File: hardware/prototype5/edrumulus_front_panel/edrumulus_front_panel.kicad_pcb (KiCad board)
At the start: 2 copper layers, 65 x 56.5 mm, 2 parts, among them J2 Raspberry Pi GPIO pins

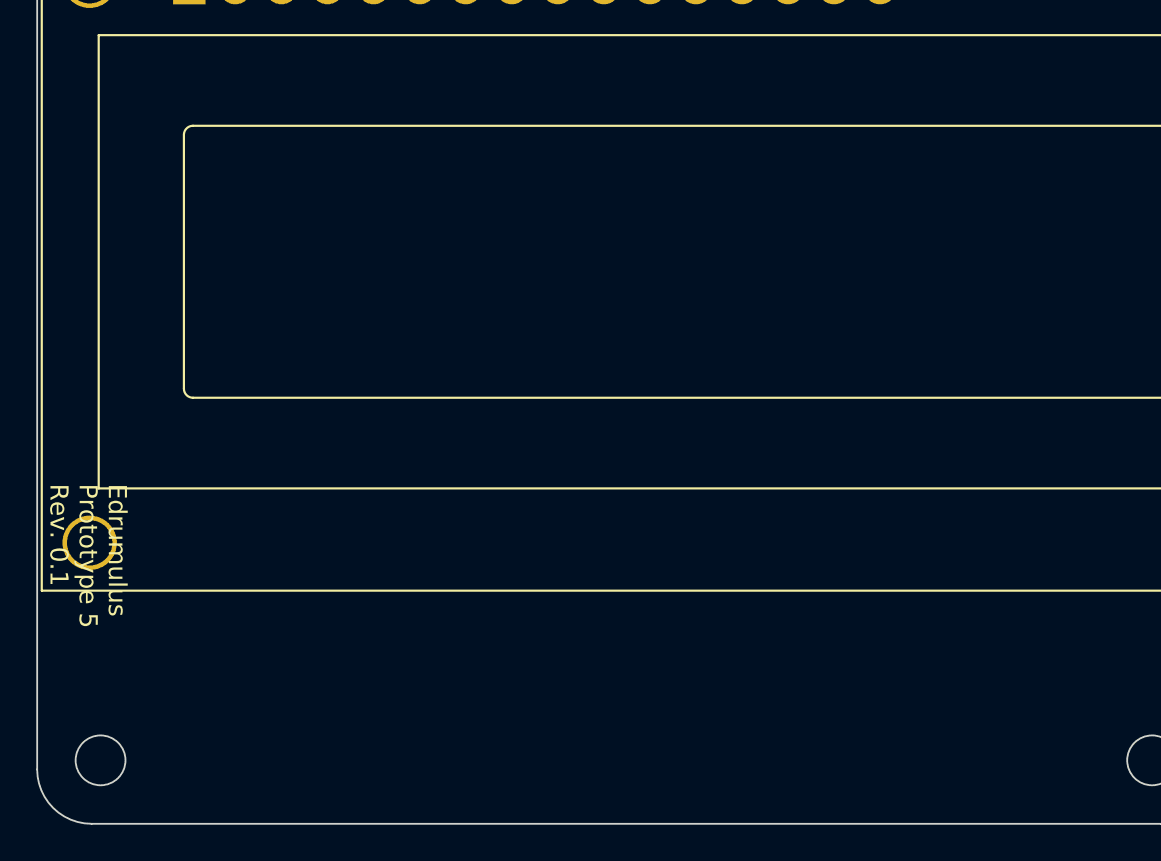
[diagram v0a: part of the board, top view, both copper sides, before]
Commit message: adding buttons to the front panel for prototype 5
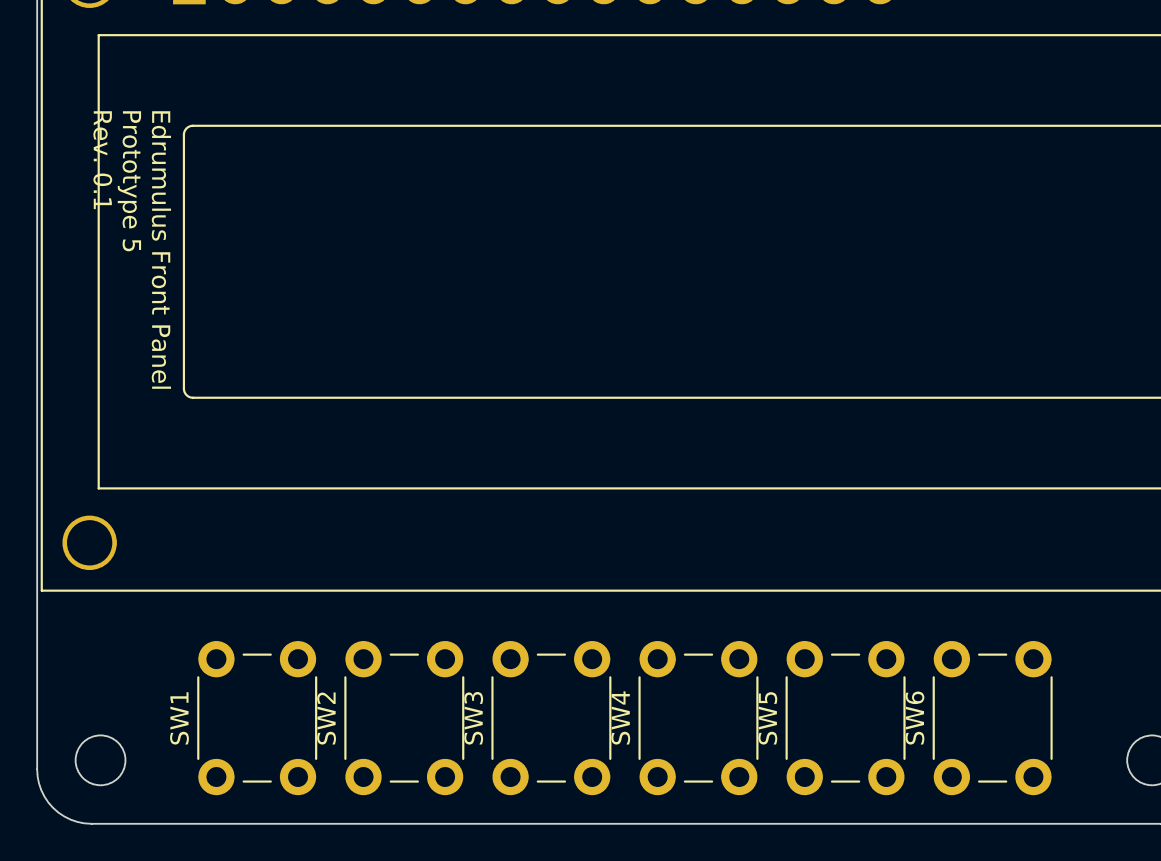
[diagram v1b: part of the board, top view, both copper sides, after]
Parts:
- added SW1: SW_Push, Button_Switch_THT:SW_PUSH_6mm_H7.3mm, F.Cu at (116.5, 127.0)
- added SW2: SW_Push, Button_Switch_THT:SW_PUSH_6mm_H7.3mm, F.Cu at (124.6, 127.0)
- added SW3: SW_Push, Button_Switch_THT:SW_PUSH_6mm_H7.3mm, F.Cu at (132.7, 127.0)
- added SW4: SW_Push, Button_Switch_THT:SW_PUSH_6mm_H7.3mm, F.Cu at (140.8, 127.0)
- added SW5: SW_Push, Button_Switch_THT:SW_PUSH_6mm_H7.3mm, F.Cu at (148.9, 127.0)
- added SW6: SW_Push, Button_Switch_THT:SW_PUSH_6mm_H7.3mm, F.Cu at (157.0, 127.0)
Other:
- board text added: "Edrumulus Front Panel Prototype 5 Rev. 0.1"
- board text removed: "Edrumulus Prototype 5 Rev. 0.1"

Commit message: work on display for prototype 5
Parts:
- added R1: 10k, Resistor_SMD:R_1206_3216Metric_Pad1.30x1.75mm_HandSolder, F.Cu at (111.8, 135.9)
- added R10: 1k, Resistor_SMD:R_1206_3216Metric_Pad1.30x1.75mm_HandSolder, F.Cu at (149.9, 113.0)
- added R11: 10k, Resistor_SMD:R_1206_3216Metric_Pad1.30x1.75mm_HandSolder, F.Cu at (150.8, 149.9)
- added R12: 1k, Resistor_SMD:R_1206_3216Metric_Pad1.30x1.75mm_HandSolder, F.Cu at (157.5, 113.0)
- added R13: 470, Resistor_SMD:R_1206_3216Metric_Pad1.30x1.75mm_HandSolder, F.Cu at (135.9, 88.9)
- added R2: 1k, Resistor_SMD:R_1206_3216Metric_Pad1.30x1.75mm_HandSolder, F.Cu at (116.8, 113.0)
- added R3: 10k, Resistor_SMD:R_1206_3216Metric_Pad1.30x1.75mm_HandSolder, F.Cu at (126.8, 137.2)
- added R4: 1k, Resistor_SMD:R_1206_3216Metric_Pad1.30x1.75mm_HandSolder, F.Cu at (124.5, 113.0)
- added R5: 10k, Resistor_SMD:R_1206_3216Metric_Pad1.30x1.75mm_HandSolder, F.Cu at (175.3, 141.0)
- added R6: 1k, Resistor_SMD:R_1206_3216Metric_Pad1.30x1.75mm_HandSolder, F.Cu at (133.3, 113.0)
- added R7: 10k, Resistor_SMD:R_1206_3216Metric_Pad1.30x1.75mm_HandSolder, F.Cu at (158.8, 144.8)
- added R8: 1k, Resistor_SMD:R_1206_3216Metric_Pad1.30x1.75mm_HandSolder, F.Cu at (141.0, 113.3)
- added R9: 10k, Resistor_SMD:R_1206_3216Metric_Pad1.30x1.75mm_HandSolder, F.Cu at (162.6, 135.9)
- added RV1: 10k, Potentiometer_THT:Potentiometer_ACP_CA9-H2,5_Horizontal, F.Cu at (184.2, 121.9)
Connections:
- DS1 pad 1: unconnected-(DS1-Pad1) -> GND
- DS1 pad 11: unconnected-(DS1-Pad11) -> PI-GPIO22
- DS1 pad 12: unconnected-(DS1-Pad12) -> PI-GPIO23
- DS1 pad 13: unconnected-(DS1-Pad13) -> PI-GPIO24
- DS1 pad 14: unconnected-(DS1-Pad14) -> PI-GPIO10
- DS1 pad 15: unconnected-(DS1-Pad15) -> Net-(DS1-Pad15)
- DS1 pad 16: unconnected-(DS1-Pad16) -> GND
- DS1 pad 2: unconnected-(DS1-Pad2) -> 5V
- DS1 pad 3: unconnected-(DS1-Pad3) -> Net-(RV1-Pad2)
- DS1 pad 4: unconnected-(DS1-Pad4) -> PI-GPIO27
- DS1 pad 5: unconnected-(DS1-Pad5) -> GND
- DS1 pad 6: unconnected-(DS1-Pad6) -> PI-GPIO17
- J2 pad 1: unconnected-(J2-Pad1) -> 3V3
- J2 pad 10: ESP-UART0-TX -> unconnected-(J2-Pad10)
- J2 pad 11: unconnected-(J2-Pad11) -> PI-GPIO17
- J2 pad 13: unconnected-(J2-Pad13) -> PI-GPIO27
- J2 pad 15: unconnected-(J2-Pad15) -> PI-GPIO22
- J2 pad 16: unconnected-(J2-Pad16) -> PI-GPIO23
- J2 pad 18: unconnected-(J2-Pad18) -> PI-GPIO24
- J2 pad 19: unconnected-(J2-Pad19) -> PI-GPIO10
- J2 pad 2: RASPI-VIN -> 5V
- J2 pad 21: PI-GPIO9 -> unconnected-(J2-Pad21)
- J2 pad 22: unconnected-(J2-Pad22) -> PI-GPIO25
- J2 pad 23: unconnected-(J2-Pad23) -> PI-GPIO11
- J2 pad 24: unconnected-(J2-Pad24) -> PI-GPIO8
- J2 pad 26: unconnected-(J2-Pad26) -> PI-GPIO7
- J2 pad 32: unconnected-(J2-Pad32) -> PI-GPIO12
- J2 pad 33: unconnected-(J2-Pad33) -> PI-GPIO13
- J2 pad 4: RASPI-VIN -> 5V
- J2 pad 7: PI-GPIO4 -> unconnected-(J2-Pad7)
- J2 pad 8: ESP-UART0-RX -> unconnected-(J2-Pad8)
- SW1 pad 1: unconnected-(SW1-Pad1) -> Net-(R1-Pad2)
- SW1 pad 2: unconnected-(SW1-Pad2) -> GND
- SW2 pad 1: unconnected-(SW2-Pad1) -> Net-(R3-Pad2)
- SW2 pad 2: unconnected-(SW2-Pad2) -> GND
- SW3 pad 1: unconnected-(SW3-Pad1) -> Net-(R5-Pad2)
- SW3 pad 2: unconnected-(SW3-Pad2) -> GND
- SW4 pad 1: unconnected-(SW4-Pad1) -> Net-(R7-Pad2)
- SW4 pad 2: unconnected-(SW4-Pad2) -> GND
- SW5 pad 1: unconnected-(SW5-Pad1) -> Net-(R10-Pad1)
- SW5 pad 2: unconnected-(SW5-Pad2) -> GND
- SW6 pad 1: unconnected-(SW6-Pad1) -> Net-(R11-Pad2)
- SW6 pad 2: unconnected-(SW6-Pad2) -> GND

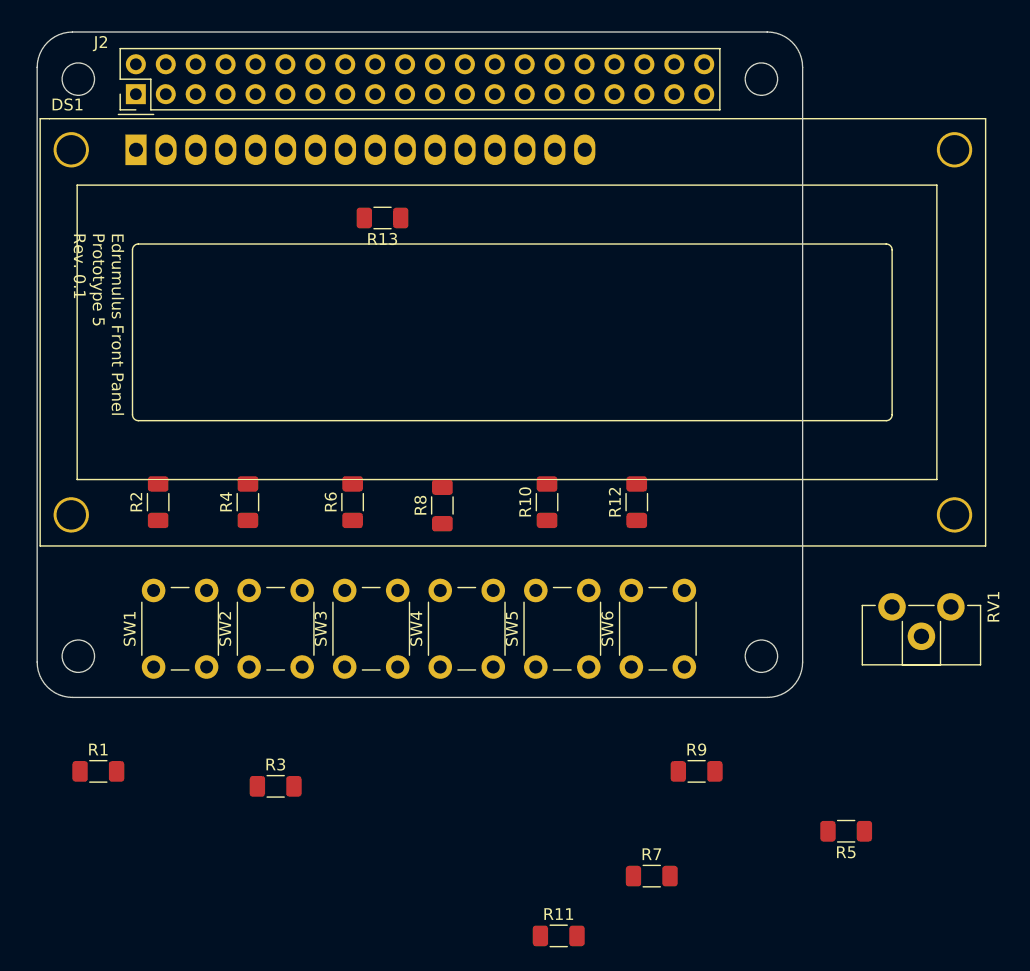
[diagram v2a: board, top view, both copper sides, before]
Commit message: finished display front panel for prototype 5
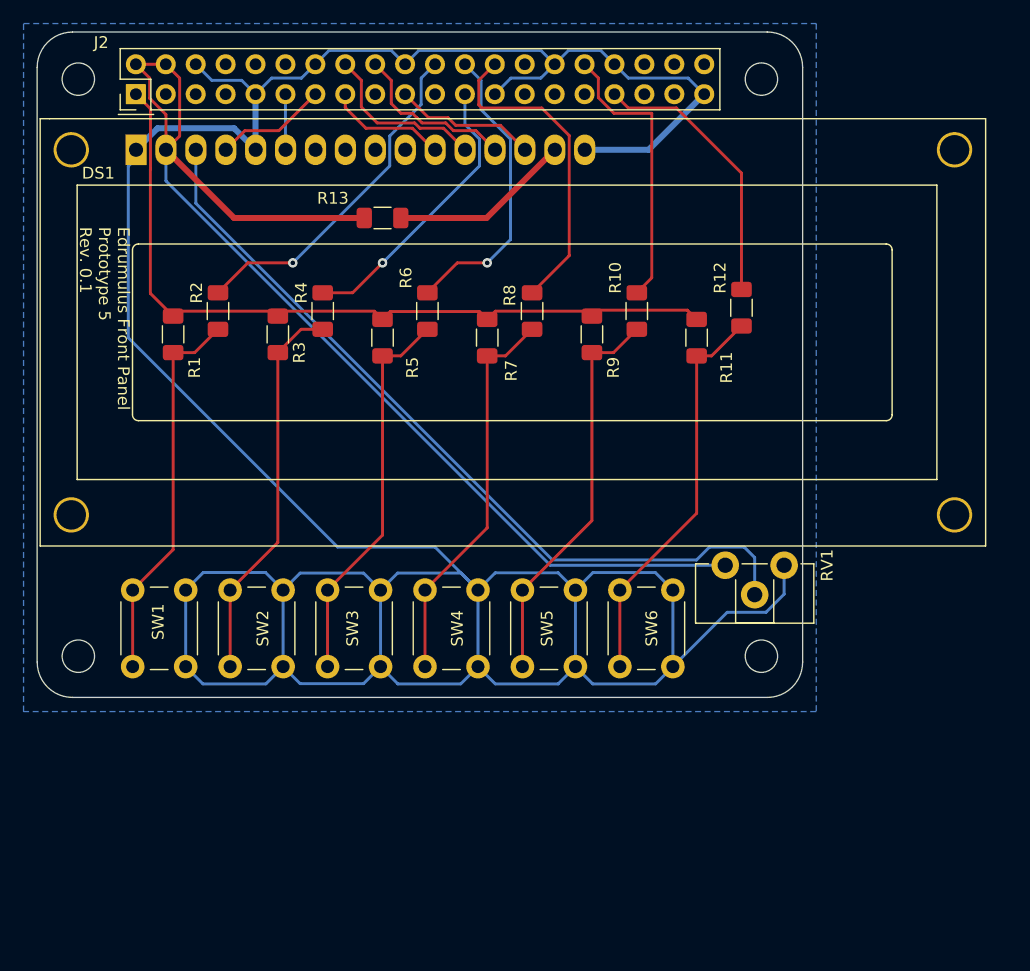
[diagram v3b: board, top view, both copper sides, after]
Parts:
- moved R5 57.5 mm to (135.9, 99.1), turned to -90 degrees
- moved R11 52.1 mm to (162.6, 99.1), turned to -90 degrees
- moved R7 47.8 mm to (144.8, 99.1), turned to -90 degrees
- moved R3 38.4 mm to (127.0, 98.8), turned to -90 degrees
- moved R9 38.2 mm to (153.7, 98.8), turned to -90 degrees
- moved R1 37.6 mm to (118.1, 98.8), turned to -90 degrees
- moved R12 18.8 mm to (166.4, 96.5)
- moved R8 18.2 mm to (148.6, 96.8)
- moved R10 17.9 mm to (157.5, 96.8)
- moved R4 17.4 mm to (130.8, 96.8)
- moved R6 17.4 mm to (139.7, 96.8)
- moved R2 17.0 mm to (121.9, 96.8)
- moved RV1 14.6 mm to (170.0, 118.4)
- moved SW1 1.78 mm to (114.7, 127.0)
- moved SW2 1.62 mm to (123.0, 127.0)
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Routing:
- net GND: track 0.00 -> 287.0 mm
- net 5V: track 0.00 -> 102.0 mm
- net Net-(RV1-Pad2): track 0.00 -> 68.5 mm
- net 3V3: track 0.00 -> 67.0 mm
- net Net-(R11-Pad2): track 0.00 -> 33.9 mm
- net Net-(R10-Pad1): track 0.00 -> 33.7 mm
- net Net-(R7-Pad2): track 0.00 -> 33.3 mm
- net Net-(R5-Pad2): track 0.00 -> 33.1 mm
- net Net-(R3-Pad2): track 0.00 -> 33.0 mm
- net Net-(R1-Pad2): track 0.00 -> 32.7 mm
- net PI-GPIO25: track 0.00 -> 29.3 mm, vias 0 -> 1
- net PI-GPIO7: track 0.00 -> 27.4 mm
- net PI-GPIO8: track 0.00 -> 25.4 mm, vias 0 -> 1
- net PI-GPIO11: track 0.00 -> 24.4 mm, vias 0 -> 1
- net PI-GPIO12: track 0.00 -> 24.2 mm
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- added copper zone on B.Cu, net GND
